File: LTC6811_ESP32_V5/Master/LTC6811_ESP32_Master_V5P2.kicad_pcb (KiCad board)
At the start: 2 copper layers, 200 x 55 mm, 325 parts, among them J10 B7B-XH-A, J11 B7B-XH-A, J12 B7B-XH-A, J13 B7B-XH-A, J18 Hole /NC, J19 Hole /NC, J21 Hole /NC, J23 CAN, J3 Hole /NC, J4 Hole /NC, J5 CAN, J6 B2P-VH-B, J7 Hole /NC, Q1 NSV1C201MZ4, Q10 TSM2323, Q11 TSM2323, Q12 TSM2323, Q13 TSM2323, Q14 NSV1C201MZ4, Q15 TSM2323, Q16 TSM2323, Q17 TSM2323, Q18 TSM2323, Q19 TSM2323, Q2 TSM2323, Q20 TSM2323, Q21 TSM2323, Q22 TSM2323, Q23 TSM2323, Q24 TSM2323, Q25 TSM2323, Q26 TSM2323, Q3 TSM2323, Q4 TSM2323, Q5 TSM2323, Q6 TSM2323, Q7 TSM2323, Q8 TSM2323, Q9 TSM2323, SW1 SW_DIP_x08, U1 MCP23017T-E/SO, U11 LTC6811HG-1, U12 LTC6811HG-1, U2 MCP2562T-E/SN, U3 BD33FC0FP-E2, U4 BD50FC0FP-E2, U8 ESP32-DevKitC V4, U9 LTC6820

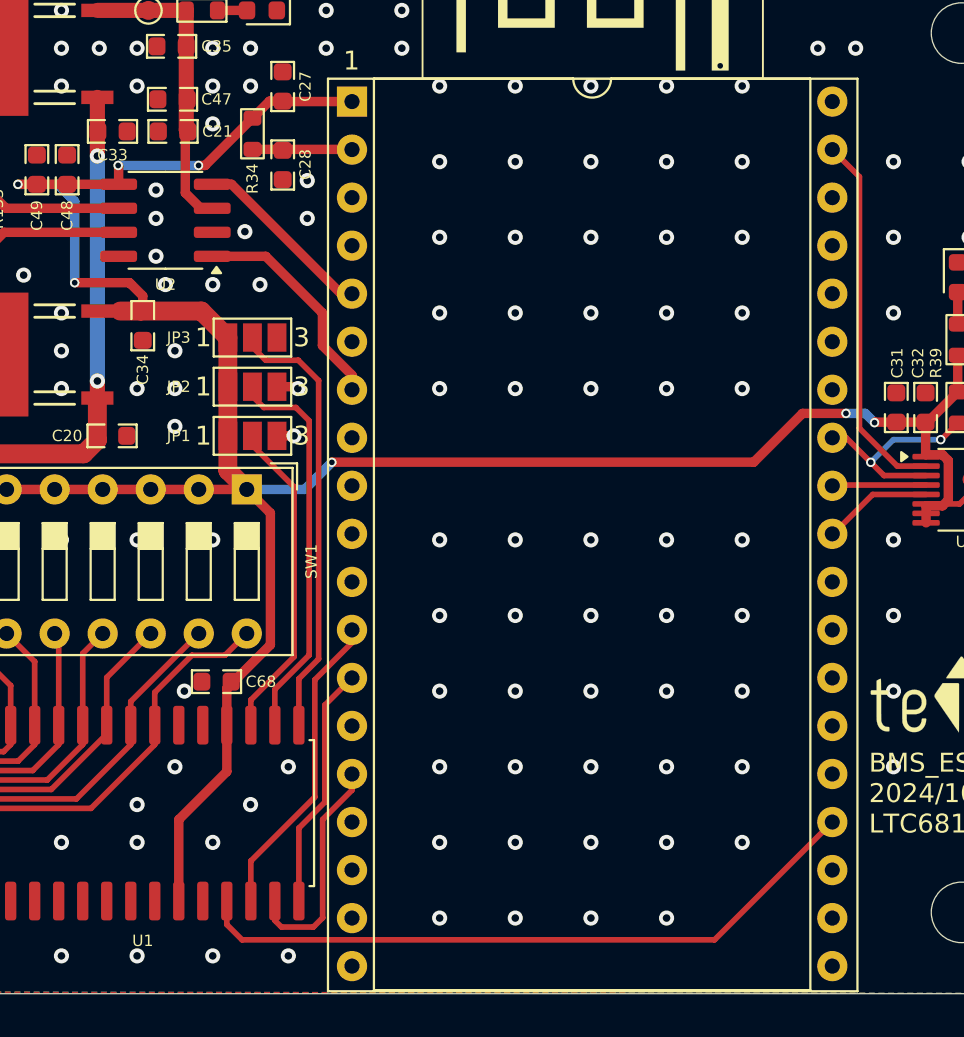
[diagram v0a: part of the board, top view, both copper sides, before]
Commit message: Connect 5V and correct GND
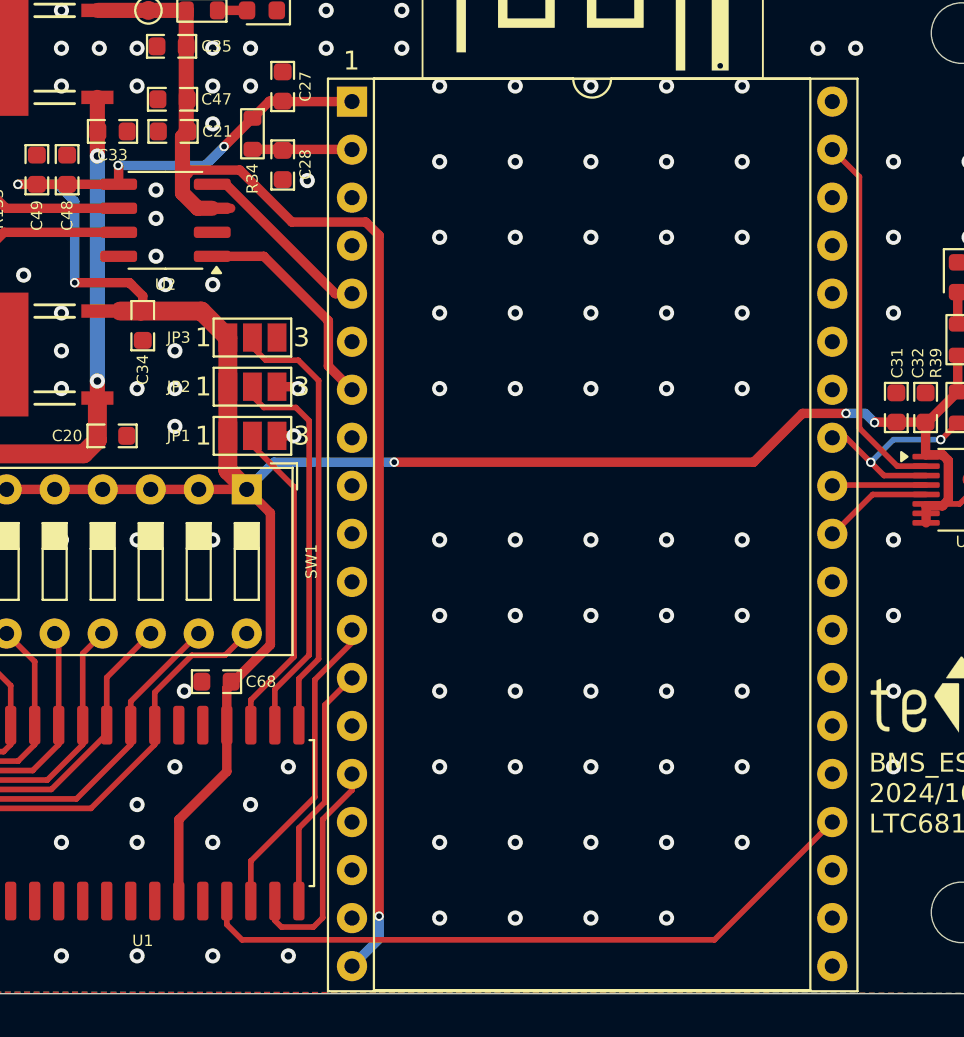
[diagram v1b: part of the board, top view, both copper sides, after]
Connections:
- U8 pad 19: /MCU/5V -> +5V
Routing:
- net +5V: track 16.2 -> 68.6 mm, vias 0 -> 1
- net GND: vias 163 -> 160
